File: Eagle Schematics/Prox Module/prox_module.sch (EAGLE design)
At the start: 45 parts, among them IC1 74LS14N, IC2 74LS14N, Q1 16MHZ

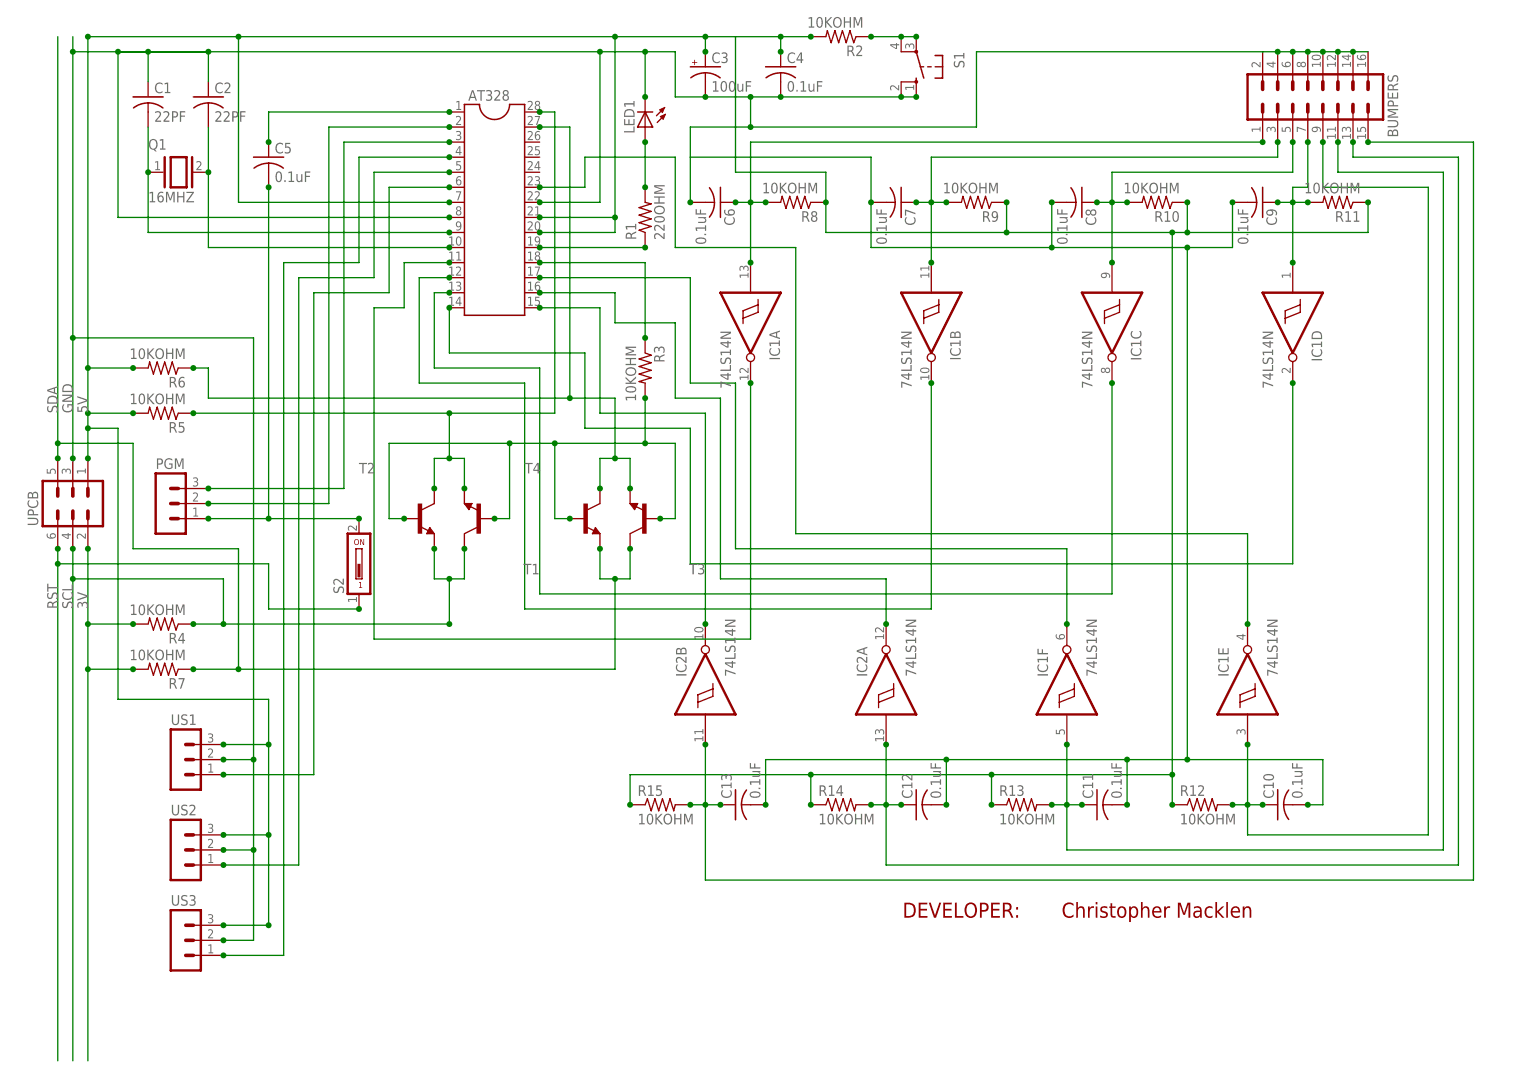
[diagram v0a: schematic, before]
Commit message: Updated prox module schematic
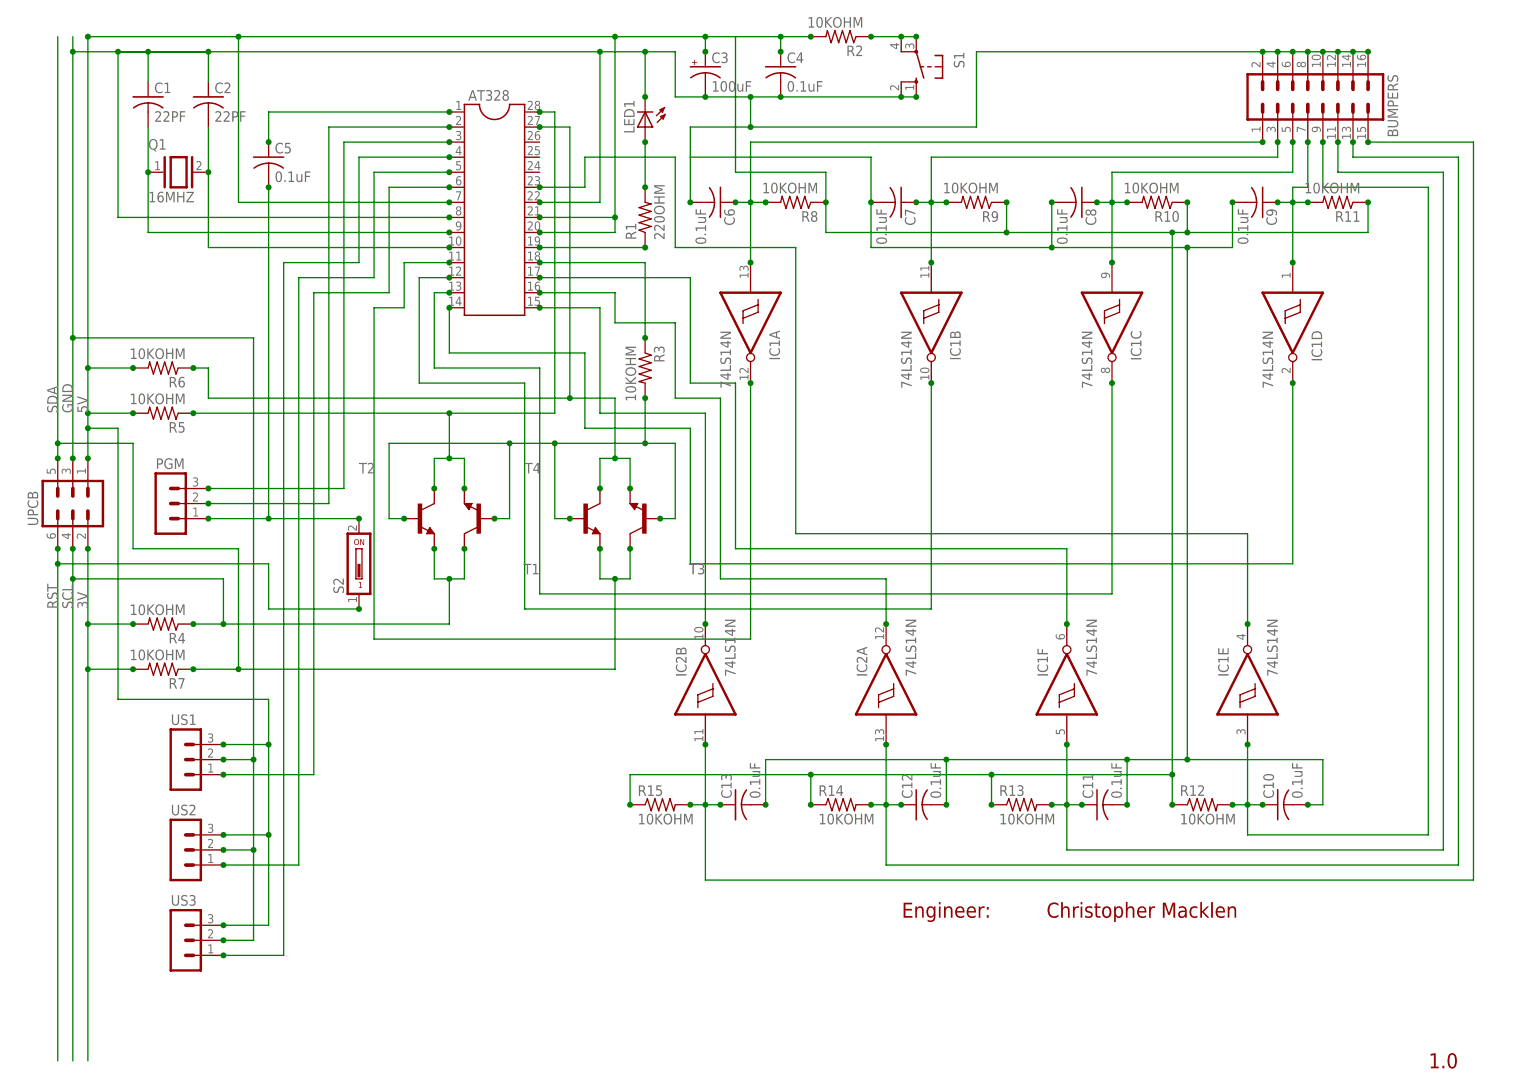
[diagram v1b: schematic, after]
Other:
- note added: "1.0"
- note added: "Engineer:"
- note removed: "DEVELOPER:"
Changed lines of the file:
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@@
 <sheet>
 <plain>
-<text x="160.02" y="33.02" size="2.54" layer="94" font="vector" align="center">DEVELOPER:</text>
-<text x="193.04" y="33.02" size="2.54" layer="94" font="vector" align="center">Christopher Macklen</text>
+<text x="190.5" y="33.02" size="2.54" layer="94" font="vector" align="center">Christopher Macklen</text>
+<text x="241.3" y="7.62" size="2.54" layer="94" font="vector" align="center">1.0</text>
+<text x="157.48" y="33.02" size="2.54" layer="94" font="vector" align="center">Engineer:</text>
 </plain>
 <instances>
@@
 <pinref part="C4" gate="G$1" pin="2"/>
 <junction x="129.54" y="170.18"/>
+<junction x="210.82" y="177.8"/>
+<junction x="228.6" y="177.8"/>
 </segment>
 </net>
@@
 <pinref part="R4" gate="G$1" pin="1"/>
 <wire x1="30.48" y1="81.28" x2="35.56" y2="81.28" width="0.1524" layer="91"/>
-<junction x="73.66" y="81.28"/>
 <junction x="30.48" y="81.28"/>
 <wire x1="35.56" y1="81.28" x2="73.66" y2="81.28" width="0.1524" layer="91"/>
@@
 <junction x="43.18" y="60.96"/>
 <junction x="43.18" y="45.72"/>
-<junction x="43.18" y="30.48"/>
 <junction x="35.56" y="60.96"/>
 <junction x="35.56" y="45.72"/>

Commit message: Fixed issue with level converter
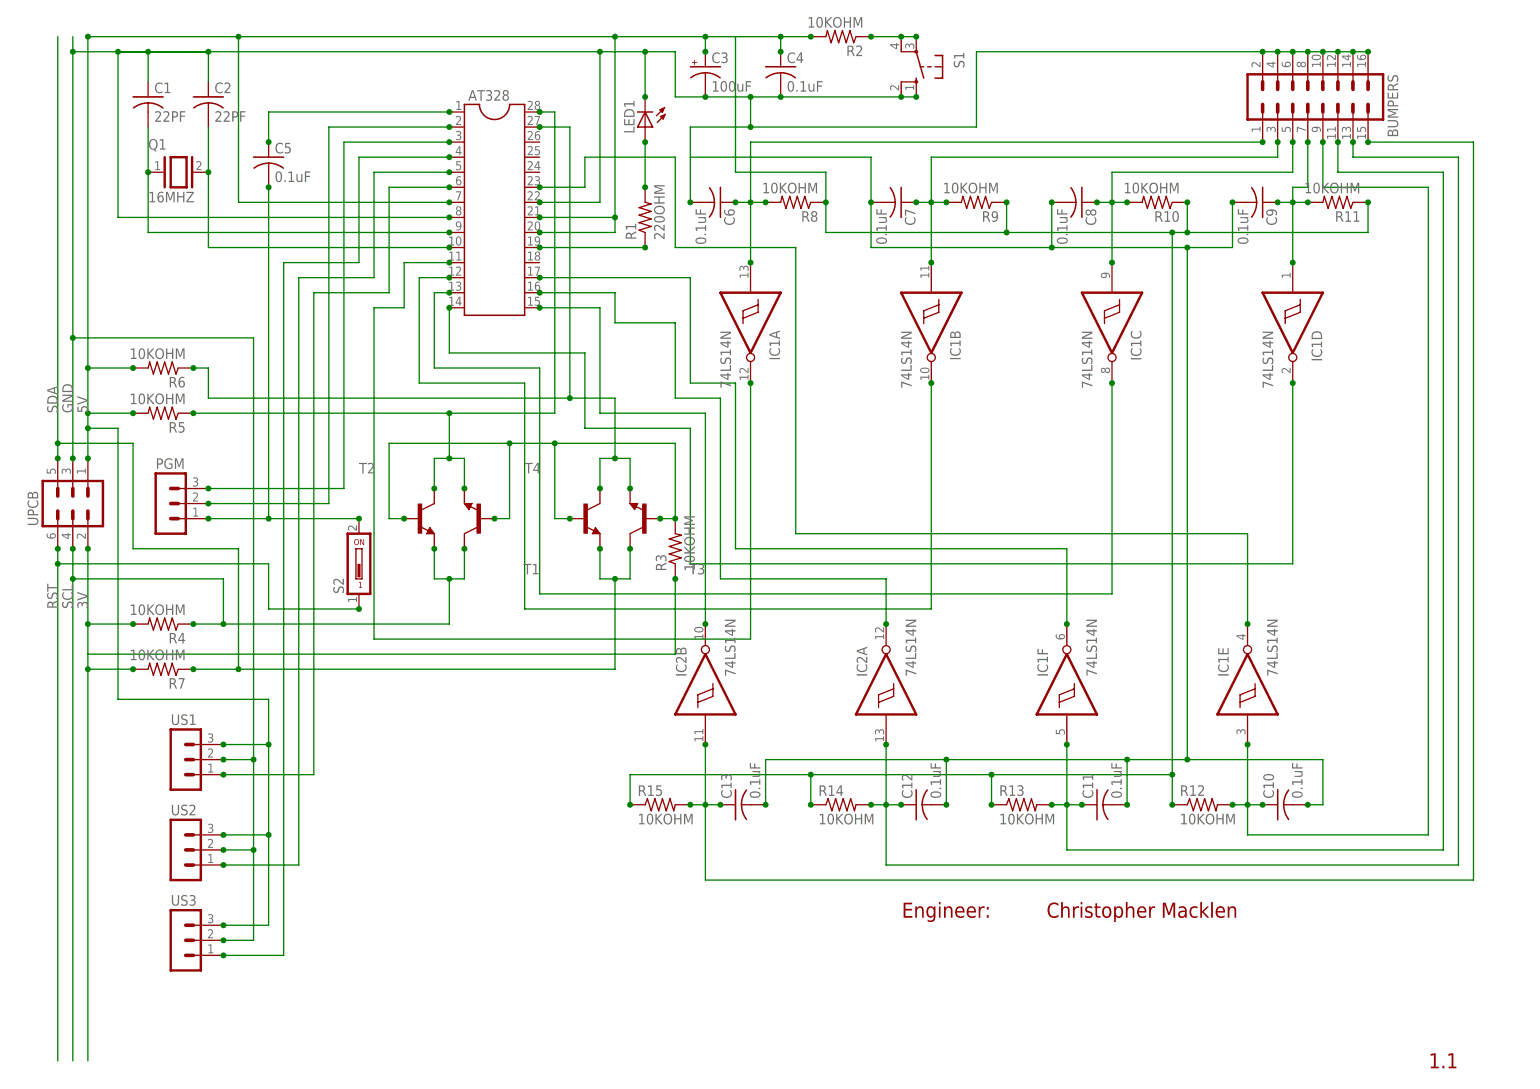
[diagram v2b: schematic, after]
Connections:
- removed net I2C-EN-1: AT328.18, R3.1
- net 3V: now also R3.1
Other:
- note added: "1.1"
- note removed: "1.0"
- moved on the sheet: R3
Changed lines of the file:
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@@
 <plain>
 <text x="190.5" y="33.02" size="2.54" layer="94" font="vector" align="center">Christopher Macklen</text>
-<text x="241.3" y="7.62" size="2.54" layer="94" font="vector" align="center">1.0</text>
+<text x="241.3" y="7.62" size="2.54" layer="94" font="vector" align="center">1.1</text>
 <text x="157.48" y="33.02" size="2.54" layer="94" font="vector" align="center">Engineer:</text>
 </plain>
@@
 <instance part="T1" gate="G$1" x="78.74" y="99.06" rot="R180"/>
 <instance part="T2" gate="G$1" x="68.58" y="99.06"/>
-<instance part="R3" gate="G$1" x="106.68" y="124.46" rot="R270"/>
+<instance part="R3" gate="G$1" x="111.76" y="93.98" rot="R90"/>
 <instance part="R4" gate="G$1" x="25.4" y="81.28" rot="R180"/>
 <instance part="R5" gate="G$1" x="25.4" y="116.84" rot="R180"/>
@@
 <junction x="12.7" y="93.98"/>
 <pinref part="R4" gate="G$1" pin="2"/>
-<wire x1="12.7" y1="81.28" x2="12.7" y2="73.66" width="0.1524" layer="91"/>
+<wire x1="12.7" y1="81.28" x2="12.7" y2="76.2" width="0.1524" layer="91"/>
+<wire x1="12.7" y1="76.2" x2="12.7" y2="73.66" width="0.1524" layer="91"/>
 <wire x1="12.7" y1="73.66" x2="12.7" y2="7.62" width="0.1524" layer="91"/>
 <wire x1="20.32" y1="81.28" x2="12.7" y2="81.28" width="0.1524" layer="91"/>
@@
 <junction x="20.32" y="73.66"/>
 <junction x="12.7" y="73.66"/>
+<wire x1="12.7" y1="76.2" x2="111.76" y2="76.2" width="0.1524" layer="91"/>
+<wire x1="111.76" y1="76.2" x2="111.76" y2="88.9" width="0.1524" layer="91"/>
+<pinref part="R3" gate="G$1" pin="1"/>
+<junction x="111.76" y="88.9"/>
 </segment>
 </net>
@@
 <wire x1="63.5" y1="111.76" x2="83.82" y2="111.76" width="0.1524" layer="91"/>
 <wire x1="83.82" y1="111.76" x2="83.82" y2="99.06" width="0.1524" layer="91"/>
-<wire x1="91.44" y1="111.76" x2="106.68" y2="111.76" width="0.1524" layer="91"/>
+<wire x1="91.44" y1="111.76" x2="111.76" y2="111.76" width="0.1524" layer="91"/>
 <pinref part="T3" gate="G$1" pin="B"/>
-<wire x1="106.68" y1="111.76" x2="111.76" y2="111.76" width="0.1524" layer="91"/>
 <wire x1="111.76" y1="111.76" x2="111.76" y2="99.06" width="0.1524" layer="91"/>
 <wire x1="111.76" y1="99.06" x2="109.22" y2="99.06" width="0.1524" layer="91"/>
@@
 <junction x="83.82" y="111.76"/>
 <junction x="91.44" y="111.76"/>
-<junction x="106.68" y="111.76"/>
 <pinref part="R3" gate="G$1" pin="2"/>
-<wire x1="106.68" y1="111.76" x2="106.68" y2="119.38" width="0.1524" layer="91"/>
-<junction x="106.68" y="119.38"/>
 <junction x="66.04" y="99.06"/>
 <junction x="81.28" y="99.06"/>
 <junction x="93.98" y="99.06"/>
 <junction x="109.22" y="99.06"/>
-</segment>
-</net>
-<net name="I2C-EN-1" class="0">
-<segment>
-<pinref part="R3" gate="G$1" pin="1"/>
-<wire x1="106.68" y1="129.54" x2="106.68" y2="142.24" width="0.1524" layer="91"/>
-<pinref part="AT328" gate="G$1" pin="18"/>
-<wire x1="106.68" y1="142.24" x2="88.9" y2="142.24" width="0.1524" layer="91"/>
-<junction x="88.9" y="142.24"/>
-<junction x="106.68" y="129.54"/>
-</segment>
-</net>
+<junction x="111.76" y="99.06"/>
+</segment>
+</net>

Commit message: Revised design
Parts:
- removed BUMPERS: (no value), con-lstb:MA08-2
- removed S2: (no value), switch-dil:SD4-01
- added B1, B2, B3, B4, B5, B6, B7, B8: 22-23-2021, con-molex:22-23-2021
- added R16: 10KOHM, rcl:R-US_0204/7
- C3: device rcl:CPOL-US085CS-1AR -> rcl:CPOL-USE2-5
- PGM, US1, US2, US3: value (none) -> 22-23-2031; device con-lstb:MA03-1 -> con-molex:22-23-2031
- UPCB: value (none) -> 22-23-2051; device con-lstb:MA03-2 -> con-molex:22-23-2051
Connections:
- removed net RST: S2.1, UPCB.6
- net 3V: now also UPCB-4.S; no longer UPCB.2
- net 5V: now also R16.2, UPCB-2.S, US1-3.S, US2-3.S, US3-3.S; no longer UPCB.1, US1.3, US2.3, US3.3
- net BMP-DBNCE1: now also B1-2.S; no longer BUMPERS.1
- net BMP-DBNCE2: now also B2-2.S; no longer BUMPERS.3
- net BMP-DBNCE3: now also B3-2.S; no longer BUMPERS.5
- net BMP-DBNCE4: now also B4-2.S; no longer BUMPERS.7
- net BMP-DBNCE5: now also B5-2.S; no longer BUMPERS.9
- net BMP-DBNCE6: now also B6-2.S; no longer BUMPERS.11
- net BMP-DBNCE7: now also B7-2.S; no longer BUMPERS.13
- net BMP-DBNCE8: now also B8-2.S; no longer BUMPERS.15
- net GND: now also B1-1.S, B2-1.S, B3-1.S, B4-1.S, B5-1.S, B6-1.S, B7-1.S, B8-1.S, UPCB-3.S, US1-2.S, US2-2.S, US3-2.S; no longer BUMPERS.10, BUMPERS.12, BUMPERS.14, BUMPERS.16, BUMPERS.2, BUMPERS.4, BUMPERS.6, BUMPERS.8, UPCB.3, US1.2, US2.2, US3.2
- net RST-1: now also PGM-1.S, R16.1; no longer PGM.1, S2.2
- net RX-TX: now also PGM-3.S; no longer PGM.3
- net SCL: now also UPCB-5.S; no longer UPCB.4
- net SDA: now also UPCB-1.S; no longer UPCB.5
- net TX-RX: now also PGM-2.S; no longer PGM.2
- net US1DATA: now also US1-1.S; no longer US1.1
- net US2DATA: now also US2-1.S; no longer US2.1
- net US3DATA: now also US3-1.S; no longer US3.1
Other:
- note added: "1.2"
- note removed: "1.1"
- moved on the sheet: R5, R6
